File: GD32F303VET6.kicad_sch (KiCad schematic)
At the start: 37 parts, among them SW1 SKRPACE010, U7 GD32F303VET6, U8 GD25Q16ESIGR, Y1 TAXM8M4RDBCCT2T, Y2 XKXGI-SUA-32.768K

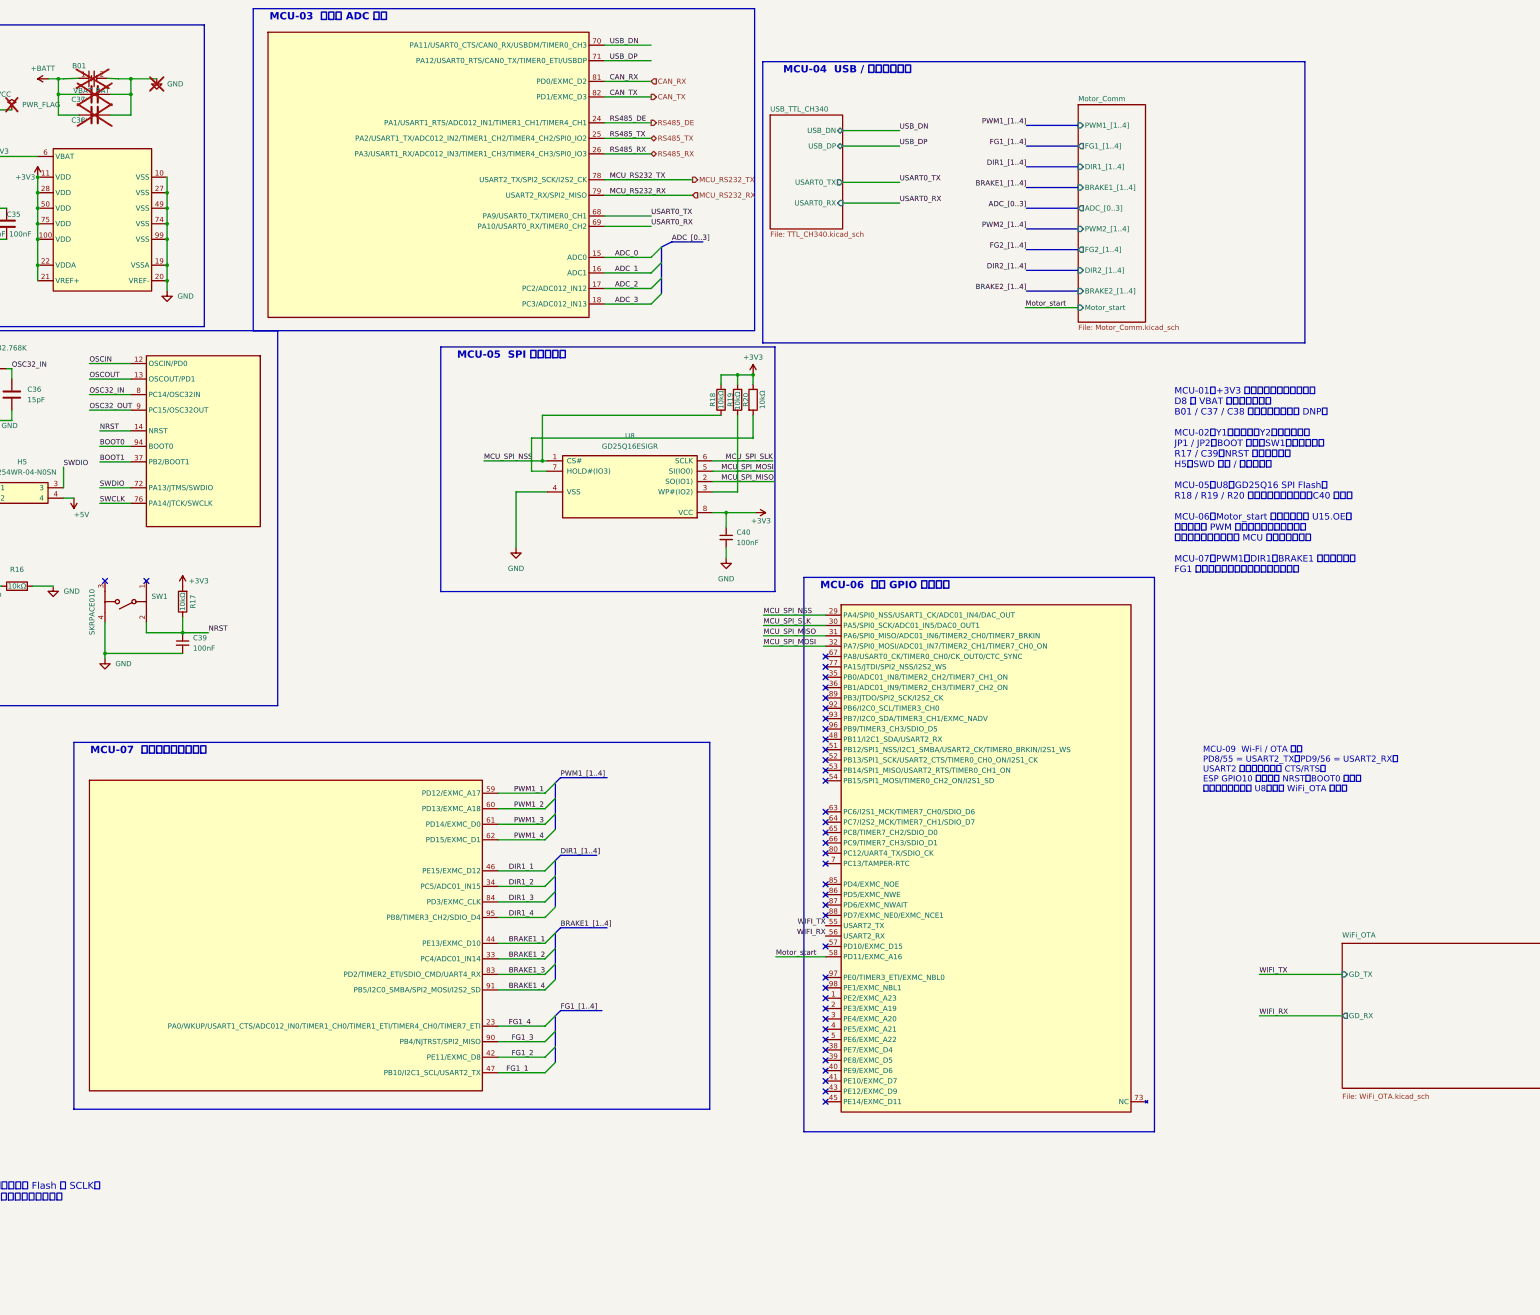
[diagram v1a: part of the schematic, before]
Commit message: 优化 MCU 符号与通道命名并同步 V2.0 PCB
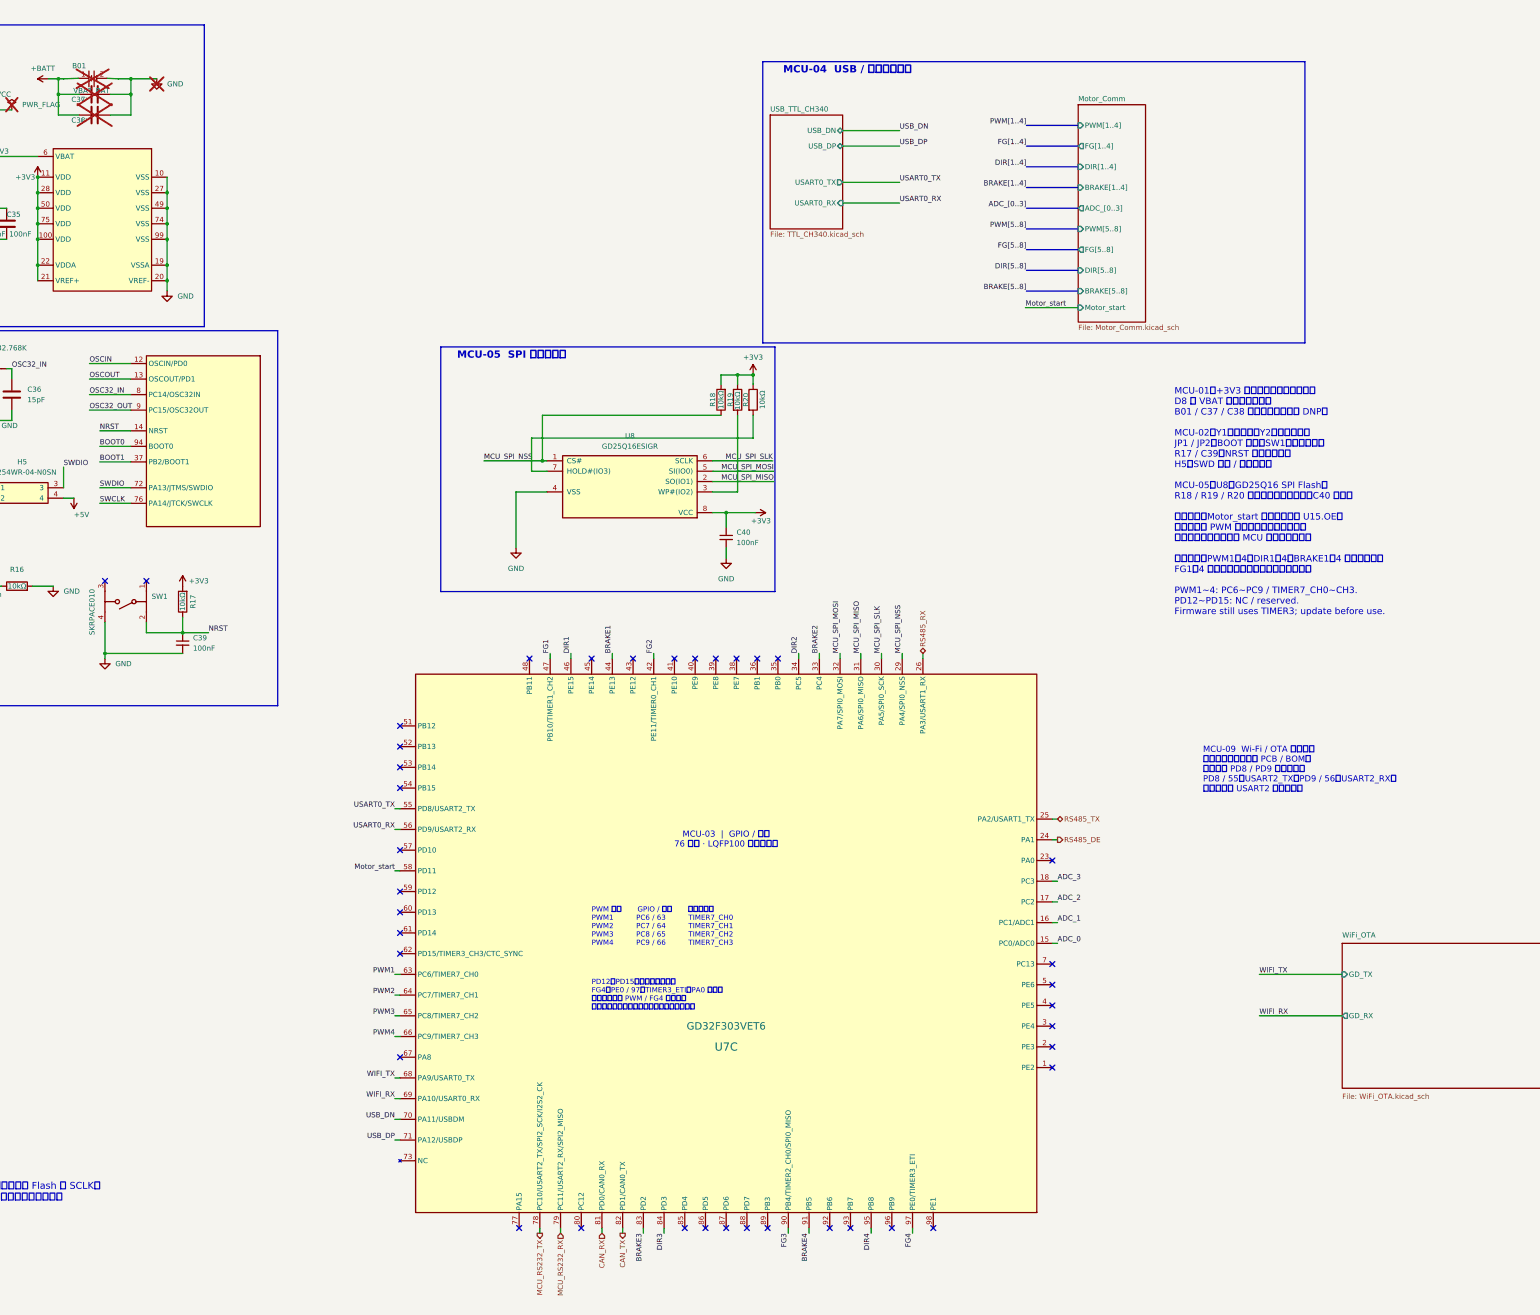
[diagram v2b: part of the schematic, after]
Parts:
- removed unit 5 of U7
- removed unit 4 of U7
- U7: symbol GD32F303VET6:GD32F303VET6_Mulit -> GD32F303VET6:GD32F303_VET6_100Pin_4Side
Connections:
- net ADC_0: now also U7.15 (PC0)
- net ADC_1: now also U7.16 (PC1)
- net ADC_2: now also U7.17 (PC2)
- net ADC_3: now also U7.18 (PC3)
- net CAN_RX: now also U7.81 (PD0/CAN0_RX)
- net CAN_TX: now also U7.82 (PD1/CAN0_TX)
- net MCU_RS232_RX: now also U7.79 (PC11)
- net MCU_RS232_TX: now also U7.78 (PC10)
- net MCU_SPI_MISO: now also U7.31 (PA6/SPI0_MISO)
- net MCU_SPI_MOSI: now also U7.32 (PA7/SPI0_MOSI)
- net MCU_SPI_NSS: now also U7.29 (PA4/SPI0_NSS)
- net MCU_SPI_SLK: now also U7.30 (PA5/SPI0_SCK)
- net Motor_start: now also U7.58 (PD11)
- net RS485_DE: now also U7.24 (PA1)
- net RS485_RX: now also U7.26 (PA3/USART1_RX)
- net RS485_TX: now also U7.25 (PA2/USART1_TX)
- net USART0_RX: now also U7.56 (PD9)
- net USART0_TX: now also U7.55 (PD8)
- net USB_DN: now also U7.70 (PA11/USBDM)
- net USB_DP: now also U7.71 (PA12/USBDP)
- net WIFI_RX: now also U7.69 (PA10/USART0_RX)
- net WIFI_TX: now also U7.68 (PA9/USART0_TX)
- net BRAKE1_1 renamed BRAKE1
- net BRAKE1_2 renamed BRAKE2
- net BRAKE1_3 renamed BRAKE3
- net BRAKE1_4 renamed BRAKE4
- net DIR1_1 renamed DIR1
- net DIR1_2 renamed DIR2
- net DIR1_3 renamed DIR3
- net DIR1_4 renamed DIR4
- net FG1_1 renamed FG1
- net FG1_2 renamed FG2
- net FG1_3 renamed FG3
- net FG1_4: no longer names the net of U7.23 (PA0)
- net PWM1_1: no longer names the net of U7.59 (PD12)
- net PWM1_2: no longer names the net of U7.60 (PD13)
- net PWM1_3: no longer names the net of U7.61 (PD14)
- net PWM1_4: no longer names the net of U7.62 (PD15)
- new net FG4: U7.97 (PE0/TIMER3_ETI)
- new net PWM1: U7.63 (PC6/TIMER7_CH0)
- new net PWM2: U7.64 (PC7/TIMER7_CH1)
- new net PWM3: U7.65 (PC8/TIMER7_CH2)
- new net PWM4: U7.66 (PC9/TIMER7_CH3)
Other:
- sheet Motor_Comm ports: added BRAKE[1..4], BRAKE[5..8], DIR[1..4], DIR[5..8], FG[1..4], FG[5..8], PWM[1..4], PWM[5..8]; removed BRAKE1_[1..4], BRAKE2_[1..4], DIR1_[1..4], DIR2_[1..4], FG1_[1..4], FG2_[1..4], PWM1_[1..4], PWM2_[1..4]
- note added: "MCU-01｜+3V3 供电与各电源引脚旁路。 D8 为 VBAT 供电选择支路。 B01 / C37 / C38 为备用区域，当前 DNP。 MCU-02｜Y1：主时钟；Y2：低速时钟。 JP1 / JP2：BOOT 配置；SW1：手动复位。 R17 / C39：NRST 上拉与滤波。 H5：SWD 下载 / 调试接口。 MCU-05｜U8：GD25Q16 SPI Flash。 R18 / R19 / R20 保持控制脚默认电平；C40 去耦。 电机使能｜Motor_start 输出至电机页 U15.OE。 高电平允许 PWM 电平转换；低电平关闭。 此处没有硬件锁存，需 MCU 持续维持使能。 四路电机｜PWM1～4、DIR1～4、BRAKE1～4 为控制输出； FG1～4 为测速输入，按电机通道编号对应。 PWM1~4: PC6~PC9 / TIMER7_CH0~CH3. PD12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"
- note added: "MCU-03 | GPIO / 外设 76 引脚 · LQFP100 顶视图顺序"
- note added: "MCU-09 Wi-Fi / OTA 备用接口 本版不装配，已排除 PCB / BOM。 原理图及 PD8 / PD9 连接保留。 PD8 / 55：USART2_TX；PD9 / 56：USART2_RX。 原设计使用 USART2 全重映射。"
- note added: "PD12～PD15：备用，未连接。 FG4：PE0 / 97，TIMER3_ETI；PA0 备用。 固件尚未适配 PWM / FG4 新映射。 完整复用名称保留在符号的备用引脚功能中。"
- note added: "PWM 网络 GPIO / 脚号 定时器通道 PWM1 PC6 / 63 TIMER7_CH0 PWM2 PC7 / 64 TIMER7_CH1 PWM3 PC8 / 65 TIMER7_CH2 PWM4 PC9 / 66 TIMER7_CH3"
- note removed: "MCU-01｜+3V3 供电与各电源引脚旁路。 D8 为 VBAT 供电选择支路。 B01 / C37 / C38 为备用区域，当前 DNP。 MCU-02｜Y1：主时钟；Y2：低速时钟。 JP1 / JP2：BOOT 配置；SW1：手动复位。 R17 / C39：NRST 上拉与滤波。 H5：SWD 下载 / 调试接口。 MCU-05｜U8：GD25Q16 SPI Flash。 R18 / R19 / R20 保持控制脚默认电平；C40 去耦。 MCU-06｜Motor_start 输出至电机页 U15.OE。 高电平允许 PWM 电平转换；低电平关闭。 此处没有硬件锁存，需 MCU 持续维持使能。 MCU-07｜PWM1、DIR1、BRAKE1 为控制输出； FG1 为测速输入，按电机通道编号对应。"
- note removed: "MCU-03 通信与 ADC 引脚"
- note removed: "MCU-06 扩展 GPIO 与总使能"
- note removed: "MCU-07 四路电机控制与测速"
- note removed: "MCU-09 Wi-Fi / OTA 接口 PD8/55 = USART2_TX；PD9/56 = USART2_RX。 USART2 全重映射；关闭 CTS/RTS。 ESP GPIO10 开漏控制 NRST；BOOT0 不变。 升级缓存使用现有 U8，详见 WiFi_OTA 子页。"

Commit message: 更新V2.0电路设计及0.5oz内层制造交付资料
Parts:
- added TP_GND_MCU1: GND_MCU, kicad_api_lib:TestPoint_Pad_D1.016mm, symbol Connector:TestPoint
- added TP_NRST1: NRST, TestPoint:TestPoint_Pad_D1.0mm, symbol Connector:TestPoint
- added TP_SPI_CLK1: SPI_CLK, kicad_api_lib:TestPoint_Pad_D0.762mm, symbol Connector:TestPoint
- added TP_SPI_CS1: SPI_CS, kicad_api_lib:TestPoint_Pad_D0.762mm, symbol Connector:TestPoint
- added TP_SPI_MISO1: SPI_MISO, kicad_api_lib:TestPoint_Pad_D0.762mm, symbol Connector:TestPoint
- added TP_SPI_MOSI1: SPI_MOSI, kicad_api_lib:TestPoint_Pad_D0.762mm, symbol Connector:TestPoint
- JP1: footprint (none) -> Jumper:SolderJumper-3_P1.3mm_Bridged12_RoundedPad1.0x1.5mm
- JP2: footprint (none) -> Connector_PinHeader_2.54mm:PinHeader_1x02_P2.54mm_Vertical
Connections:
- net +BATT: now also TP_GND_MCU1.1
- net MCU_SPI_MISO: now also TP_SPI_MISO1.1
- net MCU_SPI_MOSI: now also TP_SPI_MOSI1.1
- net MCU_SPI_NSS: now also TP_SPI_CS1.1
- net MCU_SPI_SLK: now also TP_SPI_CLK1.1
- net NRST: now also TP_NRST1.1
- net LED_PA15_N: now reaches U7.77 (PA15)
- net USART0_RX renamed USART2_RX
- net USART0_TX renamed USART2_TX
- no-connect marks 39 -> 38
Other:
- sheet Motor_Comm ports: added LED_PA15_N; removed none
- sheet USB_TTL_CH340 ports: added USART2_RX, USART2_TX; removed USART0_RX, USART0_TX
- note added: "MCU-01 主控供电与去耦"
- note added: "MCU-01A VBAT 备用支路【DNP】"
- note added: "MCU-02 时钟 / 启动 / 复位 / SWD"
- note added: "MCU-03 GPIO 与外设连接"
- note added: "MCU-06 接口与初始化说明"
- note added: "MCU-07 Wi-Fi / OTA 备用子页【DNP】"
- note added: "PA15 / 77 → Motor_Comm / MOT-08。 LED_PA15_N：低亮、高灭。 关闭 JTAG、保留 PA13/PA14 的 SWD。 先置输出高，再配置推挽，默认熄灭。 BUTTON_ESTOP_ENABLE 保持为 0。 USB：PA11 D- / PA12 D+。 CH340：USART2，PD8 TX / PD9 RX。 Wi-Fi 备用：USART0，PA9 TX / PA10 RX。 SPI0：PA4 NSS、PA5 SCK、PA6/7 数据。 MCU_SPI_SLK 为现有 SCLK 网络名称。 PWM1～4：PC6～PC9 / TIMER7_CH0～3。 FG4：PE0 / TIMER3_ETI；PD12～15 备用。 Motor_start：PD11，高使能 U15。 固件尚需适配当前 PWM / FG 映射。"
- note added: "SPI / MCU TEST POINTS"
- note added: "供电：+3V3 接 VDD / VDDA / VBAT；D8、B01、C37、C38 为 DNP。 Y1：主时钟；Y2：RTC 时钟；JP1 / JP2：BOOT 配置；SW1：复位。 R17 / C39：NRST 上拉及滤波；H5：SWD；U8：SPI Flash。"
- note added: "本版不装配，保持 PCB / BOM 排除属性。 UART 接 PA9 / PA10；GPIO10 未连接 NRST。 OTA/IAP 固件尚未实现。"
- note removed: "MCU-01 供电与去耦"
- note removed: "MCU-01｜+3V3 供电与各电源引脚旁路。 D8 为 VBAT 供电选择支路。 B01 / C37 / C38 为备用区域，当前 DNP。 MCU-02｜Y1：主时钟；Y2：低速时钟。 JP1 / JP2：BOOT 配置；SW1：手动复位。 R17 / C39：NRST 上拉与滤波。 H5：SWD 下载 / 调试接口。 MCU-05｜U8：GD25Q16 SPI Flash。 R18 / R19 / R20 保持控制脚默认电平；C40 去耦。 电机使能｜Motor_start 输出至电机页 U15.OE。 高电平允许 PWM 电平转换；低电平关闭。 此处没有硬件锁存，需 MCU 持续维持使能。 四路电机｜PWM1～4、DIR1～4、BRAKE1～4 为控制输出； FG1～4 为测速输入，按电机通道编号对应。 PWM1~4: PC6~PC9 / TIMER7_CH0~CH3. PD12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"
- note removed: "MCU-02 时钟 / 启动 / 调试"
- note removed: "MCU-03 | GPIO / 外设 76 引脚 · LQFP100 顶视图顺序"
- note removed: "MCU-09 Wi-Fi / OTA 备用接口 本版不装配，已排除 PCB / BOM。 原理图及 PD8 / PD9 连接保留。 PD8 / 55：USART2_TX；PD9 / 56：USART2_RX。 原设计使用 USART2 全重映射。"
- note removed: "PD12～PD15：备用，未连接。 FG4：PE0 / 97，TIMER3_ETI；PA0 备用。 固件尚未适配 PWM / FG4 新映射。 完整复用名称保留在符号的备用引脚功能中。"
- note removed: "PWM 网络 GPIO / 脚号 定时器通道 PWM1 PC6 / 63 TIMER7_CH0 PWM2 PC7 / 64 TIMER7_CH1 PWM3 PC8 / 65 TIMER7_CH2 PWM4 PC9 / 66 TIMER7_CH3"
- note removed: "接口命名说明：MCU_SPI_SLK 保留现有名称，实际连接 Flash 的 SCLK。 Motor_start 控制 PWM 通道使能；它不直接表示电机正在转动。"
